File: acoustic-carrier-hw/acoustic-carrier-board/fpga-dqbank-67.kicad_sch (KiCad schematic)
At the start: 14 parts, among them IC1 ECP5-BGA256, Y4 Crystal Oscillator

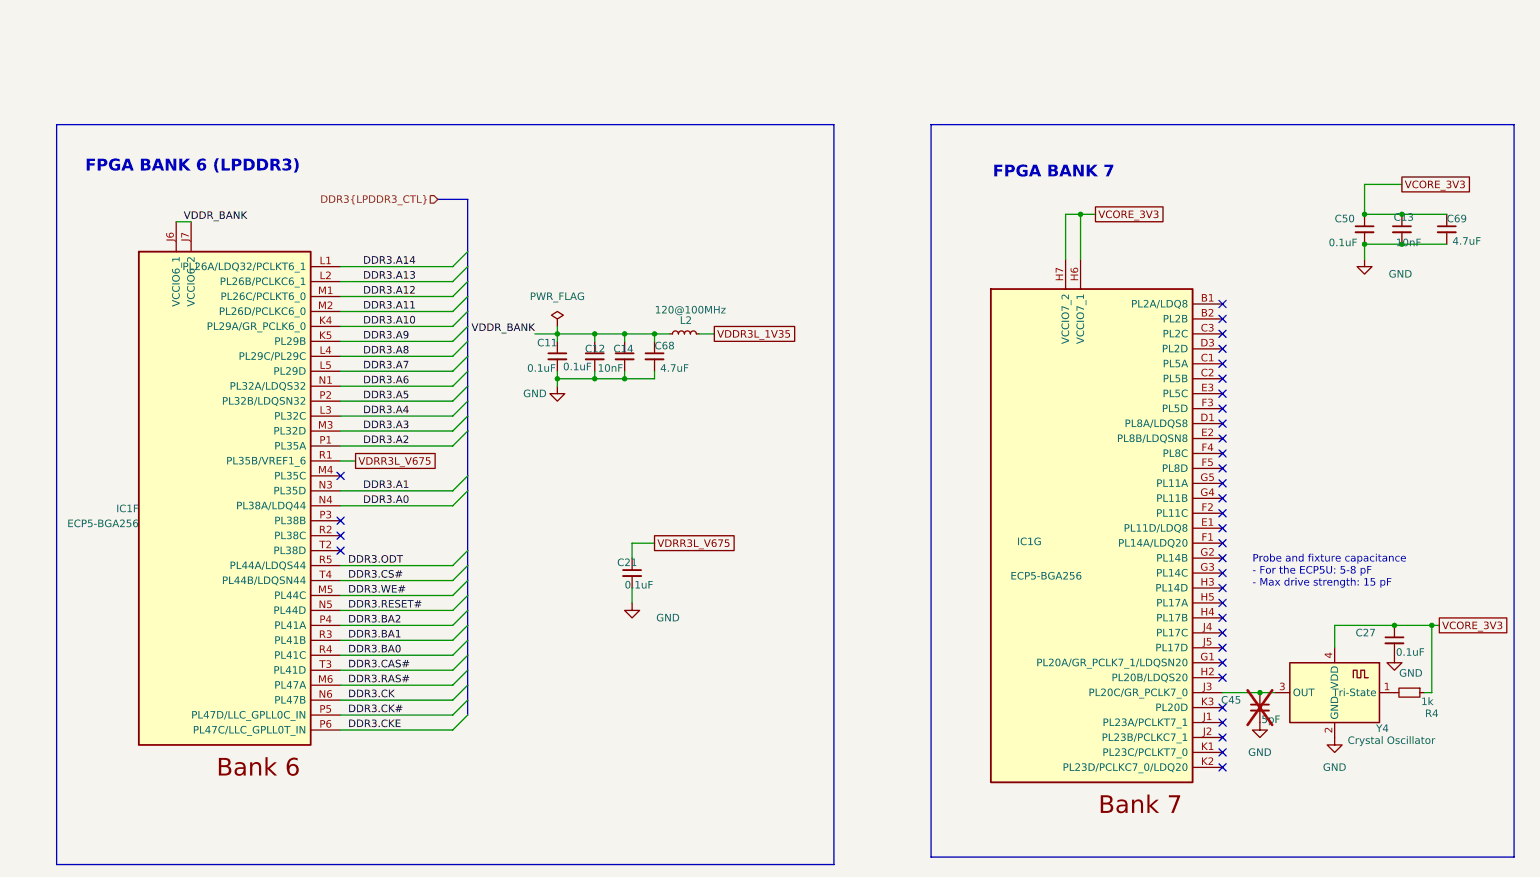
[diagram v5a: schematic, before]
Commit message: [carrier] Finished rough layout, p (put together according to component category
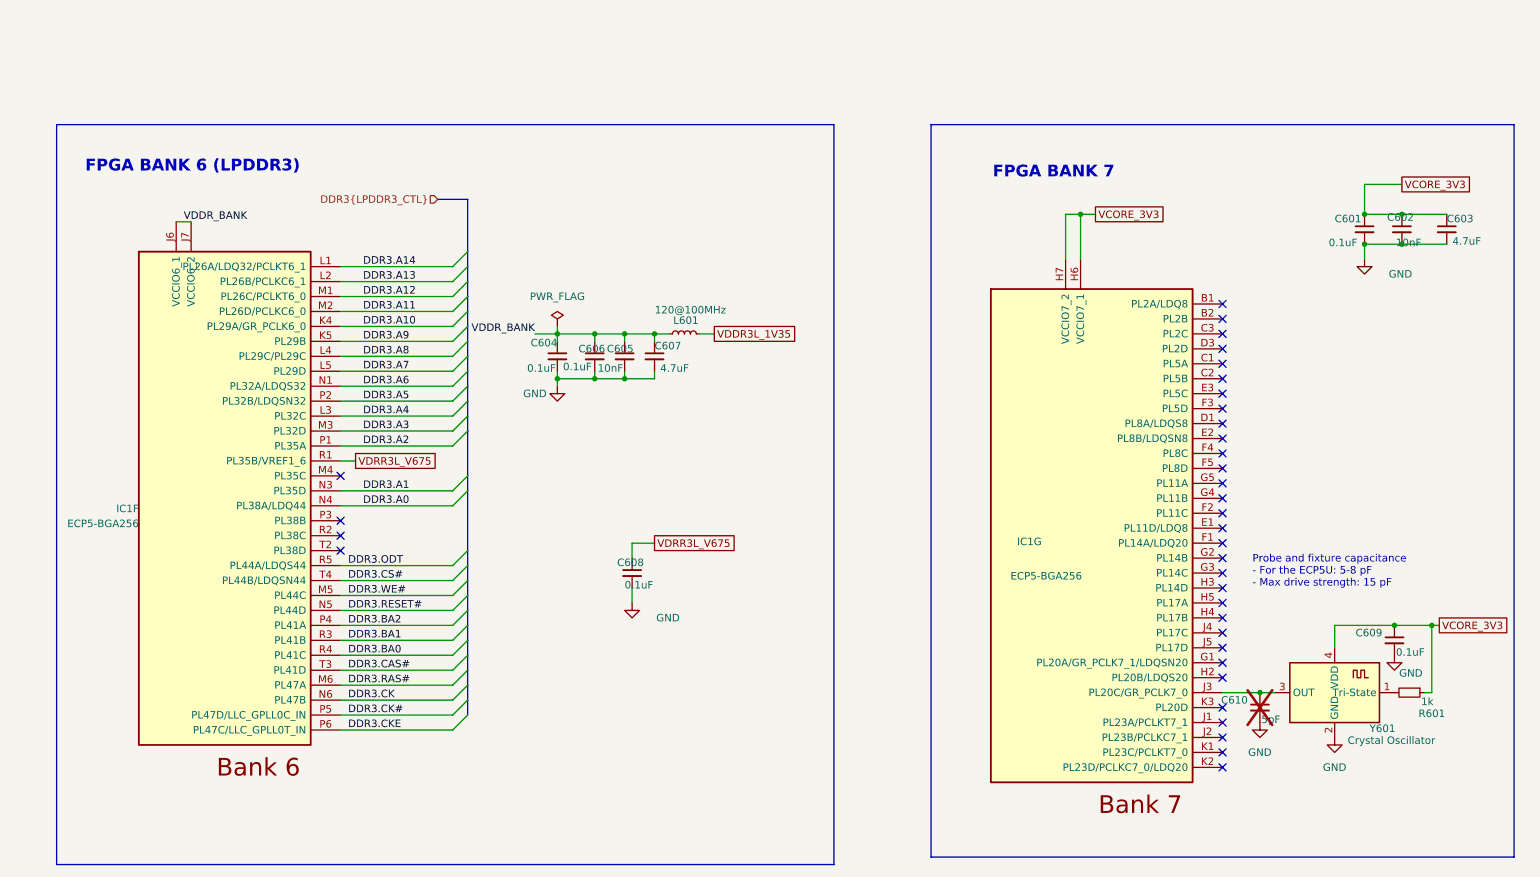
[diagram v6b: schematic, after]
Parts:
- renumbered C50 to C601, C13 to C602, C69 to C603, C11 to C604, C14 to C605, C12 to C606, C68 to C607, C21 to C608, C27 to C609, C45 to C610, L2 to L601, R4 to R601, Y4 to Y601
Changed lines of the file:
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@@
 		(dnp no)
 		(fields_autoplaced yes)
-		(property "Reference" "#PWR012"
+		(property "Reference" "#PWR0605"
 			(at 227.33 140.97 0)
 			(effects
@@
 			(project "acoustic-carrier-board"
 				(path "/25b015c9-ab13-4427-b72c-b6f348597100/9b4bf25f-717e-478b-8aa4-28cd7b267efe"
-					(reference "#PWR012")
+					(reference "#PWR0605")
 					(unit 1)
 				)
@@
 		(on_board yes)
 		(dnp no)
-		(property "Reference" "C12"
+		(property "Reference" "C606"
 			(at 116.078 71.12 0)
 			(effects
@@
 			(project "acoustic-carrier-board"
 				(path "/25b015c9-ab13-4427-b72c-b6f348597100/9b4bf25f-717e-478b-8aa4-28cd7b267efe"
-					(reference "C12")
+					(reference "C606")
 					(unit 1)
 				)
@@
 		(on_board yes)
 		(dnp no)
-		(property "Reference" "C69"
+		(property "Reference" "C603"
 			(at 259.08 49.022 0)
 			(effects
@@
 			(project "acoustic-carrier-board"
 				(path "/25b015c9-ab13-4427-b72c-b6f348597100/9b4bf25f-717e-478b-8aa4-28cd7b267efe"
-					(reference "C69")
+					(reference "C603")
 					(unit 1)
 				)
@@
 		(on_board yes)
 		(dnp no)
-		(property "Reference" "C21"
+		(property "Reference" "C608"
 			(at 118.11 107.442 0)
 			(effects
@@
 			(project "acoustic-carrier-board"
 				(path "/25b015c9-ab13-4427-b72c-b6f348597100/9b4bf25f-717e-478b-8aa4-28cd7b267efe"
-					(reference "C21")
+					(reference "C608")
 					(unit 1)
 				)
@@
 		(dnp no)
 		(fields_autoplaced yes)
-		(property "Reference" "#FLG01"
+		(property "Reference" "#FLG0601"
 			(at 107.95 65.405 0)
 			(effects
@@
 			(project "acoustic-carrier-board"
 				(path "/25b015c9-ab13-4427-b72c-b6f348597100/9b4bf25f-717e-478b-8aa4-28cd7b267efe"
-					(reference "#FLG01")
+					(reference "#FLG0601")
 					(unit 1)
 				)
@@
 		(on_board yes)
 		(dnp no)
-		(property "Reference" "#PWR07"
+		(property "Reference" "#PWR0603"
 			(at 120.65 120.65 0)
 			(effects
@@
 			(project "acoustic-carrier-board"
 				(path "/25b015c9-ab13-4427-b72c-b6f348597100/9b4bf25f-717e-478b-8aa4-28cd7b267efe"
-					(reference "#PWR07")
+					(reference "#PWR0603")
 					(unit 1)
 				)
@@
 		(on_board yes)
 		(dnp no)
-		(property "Reference" "C27"
+		(property "Reference" "C609"
 			(at 243.586 119.38 0)
 			(effects
@@
 			(project "acoustic-carrier-board"
 				(path "/25b015c9-ab13-4427-b72c-b6f348597100/9b4bf25f-717e-478b-8aa4-28cd7b267efe"
-					(reference "C27")
+					(reference "C609")
 					(unit 1)
 				)
@@
 		(on_board yes)
 		(dnp no)
-		(property "Reference" "C14"
+		(property "Reference" "C605"
 			(at 120.904 71.12 0)
 			(effects
@@
 			(project "acoustic-carrier-board"
 				(path "/25b015c9-ab13-4427-b72c-b6f348597100/9b4bf25f-717e-478b-8aa4-28cd7b267efe"
-					(reference "C14")
+					(reference "C605")
 					(unit 1)
 				)
@@
 		(on_board yes)
 		(dnp no)
-		(property "Reference" "Y4"
+		(property "Reference" "Y601"
 			(at 248.158 135.636 0)
 			(effects
@@
 			(project "acoustic-carrier-board"
 				(path "/25b015c9-ab13-4427-b72c-b6f348597100/9b4bf25f-717e-478b-8aa4-28cd7b267efe"
-					(reference "Y4")
+					(reference "Y601")
 					(unit 1)
 				)
@@
 		(dnp no)
 		(fields_autoplaced yes)
-		(property "Reference" "#PWR013"
+		(property "Reference" "#PWR0606"
 			(at 240.03 143.51 0)
 			(effects
@@
 			(project "acoustic-carrier-board"
 				(path "/25b015c9-ab13-4427-b72c-b6f348597100/9b4bf25f-717e-478b-8aa4-28cd7b267efe"
-					(reference "#PWR013")
+					(reference "#PWR0606")
 					(unit 1)
 				)
@@
 		(on_board yes)
 		(dnp no)
-		(property "Reference" "C11"
+		(property "Reference" "C604"
 			(at 107.95 70.104 0)
 			(effects
@@
 			(project "acoustic-carrier-board"
 				(path "/25b015c9-ab13-4427-b72c-b6f348597100/9b4bf25f-717e-478b-8aa4-28cd7b267efe"
-					(reference "C11")
+					(reference "C604")
 					(unit 1)
 				)
@@
 		(on_board yes)
 		(dnp no)
-		(property "Reference" "#PWR011"
+		(property "Reference" "#PWR0604"
 			(at 250.19 129.54 0)
 			(effects
@@
 			(project "acoustic-carrier-board"
 				(path "/25b015c9-ab13-4427-b72c-b6f348597100/9b4bf25f-717e-478b-8aa4-28cd7b267efe"
-					(reference "#PWR011")
+					(reference "#PWR0604")
 					(unit 1)
 				)
@@
 		(on_board yes)
 		(dnp no)
-		(property "Reference" "#PWR05"
+		(property "Reference" "#PWR0602"
 			(at 107.95 83.82 0)
 			(effects
@@
 			(project "acoustic-carrier-board"
 				(path "/25b015c9-ab13-4427-b72c-b6f348597100/9b4bf25f-717e-478b-8aa4-28cd7b267efe"
-					(reference "#PWR05")
+					(reference "#PWR0602")
 					(unit 1)
 				)
@@
 		(on_board yes)
 		(dnp no)
-		(property "Reference" "C50"
+		(property "Reference" "C601"
 			(at 240.03 49.022 0)
 			(effects
@@
 			(project "acoustic-carrier-board"
 				(path "/25b015c9-ab13-4427-b72c-b6f348597100/9b4bf25f-717e-478b-8aa4-28cd7b267efe"
-					(reference "C50")
+					(reference "C601")
 					(unit 1)
 				)
@@
 		(on_board yes)
 		(dnp no)
-		(property "Reference" "#PWR017"
+		(property "Reference" "#PWR0601"
 			(at 245.11 62.23 0)
 			(effects
@@
 			(project "acoustic-carrier-board"
 				(path "/25b015c9-ab13-4427-b72c-b6f348597100/9b4bf25f-717e-478b-8aa4-28cd7b267efe"
-					(reference "#PWR017")
+					(reference "#PWR0601")
 					(unit 1)
 				)
@@
 		(on_board yes)
 		(dnp yes)
-		(property "Reference" "C45"
+		(property "Reference" "C610"
 			(at 220.726 130.81 0)
 			(effects
@@
 			(project "acoustic-carrier-board"
 				(path "/25b015c9-ab13-4427-b72c-b6f348597100/9b4bf25f-717e-478b-8aa4-28cd7b267efe"
-					(reference "C45")
+					(reference "C610")
 					(unit 1)
 				)
@@
 		(on_board yes)
 		(dnp no)
-		(property "Reference" "C68"
+		(property "Reference" "C607"
 			(at 124.46 70.612 0)
 			(effects
@@
 			(project "acoustic-carrier-board"
 				(path "/25b015c9-ab13-4427-b72c-b6f348597100/9b4bf25f-717e-478b-8aa4-28cd7b267efe"
-					(reference "C68")
+					(reference "C607")
 					(unit 1)
 				)
@@
 		(on_board yes)
 		(dnp no)
-		(property "Reference" "L2"
+		(property "Reference" "L601"
 			(at 129.794 66.294 90)
 			(effects
@@
 			(project "acoustic-carrier-board"
 				(path "/25b015c9-ab13-4427-b72c-b6f348597100/9b4bf25f-717e-478b-8aa4-28cd7b267efe"
-					(reference "L2")
+					(reference "L601")
 					(unit 1)
 				)
@@
 		(on_board yes)
 		(dnp no)
-		(property "Reference" "C13"
+		(property "Reference" "C602"
 			(at 253.492 48.768 0)
 			(effects
@@
 			(project "acoustic-carrier-board"
 				(path "/25b015c9-ab13-4427-b72c-b6f348597100/9b4bf25f-717e-478b-8aa4-28cd7b267efe"
-					(reference "C13")
+					(reference "C602")
 					(unit 1)
 				)
@@
 		(on_board yes)
 		(dnp no)
-		(property "Reference" "R4"
+		(property "Reference" "R601"
 			(at 256.54 133.096 90)
 			(effects
@@
 			(project "acoustic-carrier-board"
 				(path "/25b015c9-ab13-4427-b72c-b6f348597100/9b4bf25f-717e-478b-8aa4-28cd7b267efe"
-					(reference "R4")
+					(reference "R601")
 					(unit 1)
 				)

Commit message: [¢arrier] Added netties and determined trace geometry for 50 ohms SE / 100 ohms DIFF impedance (next) reset the appropriate DQS group signals, RGMII and USB signals
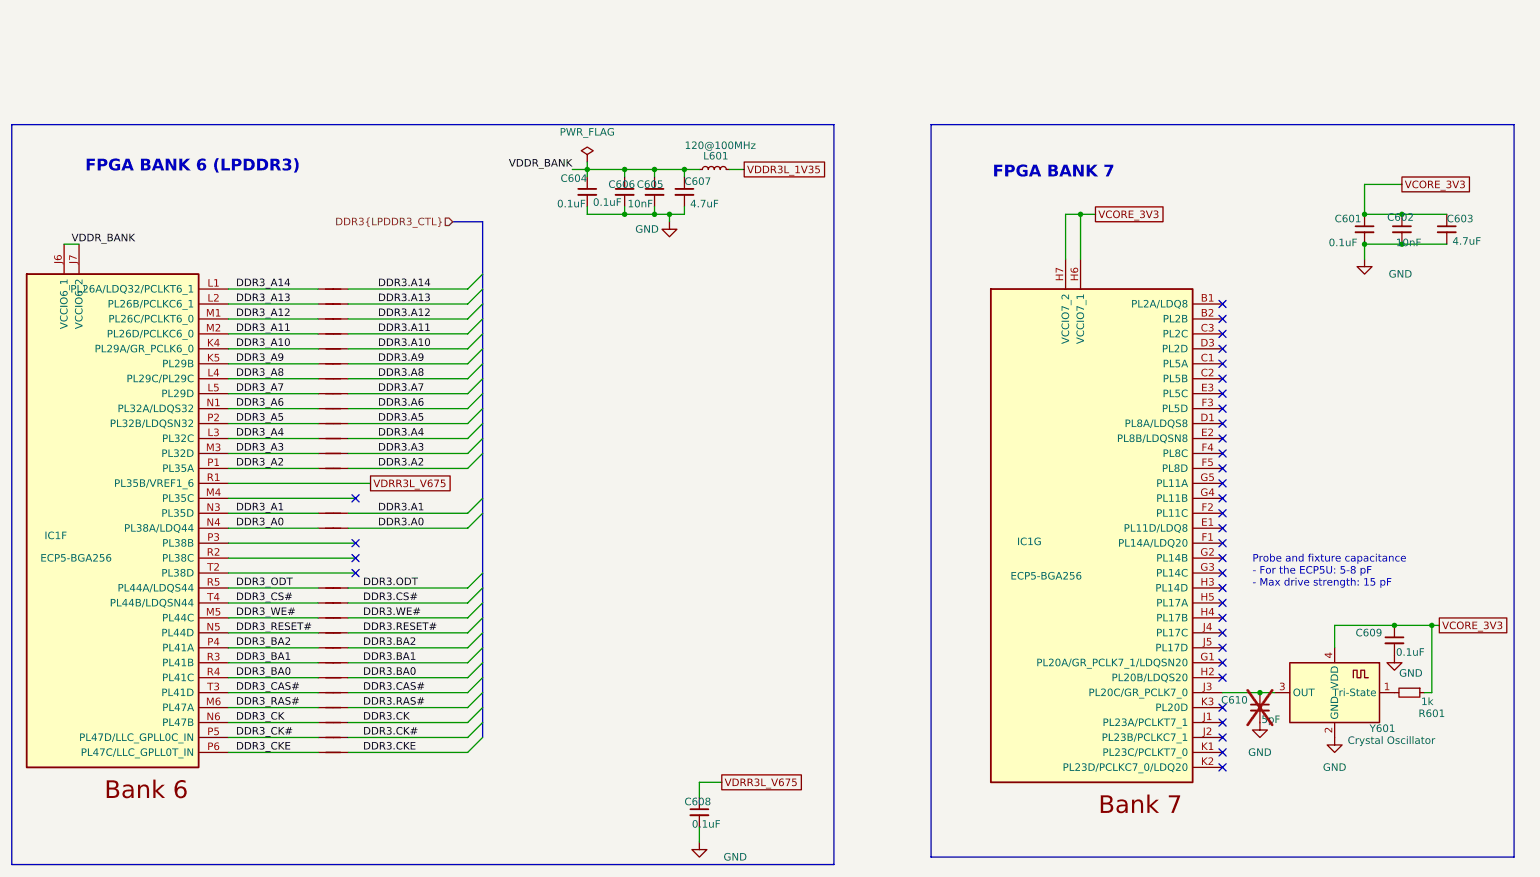
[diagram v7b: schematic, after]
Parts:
- added NT601, NT602, NT603, NT604, NT605, NT606, NT607, NT608, NT609, NT610, NT613, NT614, NT615, NT616, NT617, NT618, NT619, NT620, NT621, NT622, NT623, NT624, NT625, NT626, NT627: NetTie_2, iw-misc:NetTie-2_SMD_Pad0.1565mm, symbol Device:NetTie_2
- added NT611, NT612: NetTie_2, iw-misc:NetTie-2_SMD_Pad0.1240mm, symbol Device:NetTie_2
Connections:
- net DDR3.A0: now also NT627.2; no longer IC1.N4 (PL38A/LDQ44)
- net DDR3.A1: now also NT626.2; no longer IC1.N3 (PL35D)
- net DDR3.A10: now also NT617.2; no longer IC1.K4 (PL29A/GR_PCLK6_0)
- net DDR3.A11: now also NT616.2; no longer IC1.M2 (PL26D/PCLKC6_0)
- net DDR3.A12: now also NT615.2; no longer IC1.M1 (PL26C/PCLKT6_0)
- net DDR3.A13: now also NT614.2; no longer IC1.L2 (PL26B/PCLKC6_1)
- net DDR3.A14: now also NT613.2; no longer IC1.L1 (PL26A/LDQ32/PCLKT6_1)
- net DDR3.A2: now also NT625.2; no longer IC1.P1 (PL35A)
- net DDR3.A3: now also NT624.2; no longer IC1.M3 (PL32D)
- net DDR3.A4: now also NT623.2; no longer IC1.L3 (PL32C)
- net DDR3.A5: now also NT622.2; no longer IC1.P2 (PL32B/LDQSN32)
- net DDR3.A6: now also NT621.2; no longer IC1.N1 (PL32A/LDQS32)
- net DDR3.A7: now also NT620.2; no longer IC1.L5 (PL29D)
- net DDR3.A8: now also NT619.2; no longer IC1.L4 (PL29C/PL29C)
- net DDR3.A9: now also NT618.2; no longer IC1.K5 (PL29B)
- net DDR3.BA0: now also NT607.2; no longer IC1.R4 (PL41C)
- net DDR3.BA1: now also NT606.2; no longer IC1.R3 (PL41B)
- net DDR3.BA2: now also NT605.2; no longer IC1.P4 (PL41A)
- net DDR3.CAS#: now also NT608.2; no longer IC1.T3 (PL41D)
- net DDR3.CK: now also NT611.2; no longer IC1.N6 (PL47B)
- net DDR3.CK#: now also NT612.2; no longer IC1.P5 (PL47D/LLC_GPLL0C_IN)
- net DDR3.CKE: now also NT610.2; no longer IC1.P6 (PL47C/LLC_GPLL0T_IN)
- net DDR3.CS#: now also NT602.2; no longer IC1.T4 (PL44B/LDQSN44)
- net DDR3.ODT: now also NT601.2; no longer IC1.R5 (PL44A/LDQS44)
- net DDR3.RAS#: now also NT609.2; no longer IC1.M6 (PL47A)
- net DDR3.RESET#: now also NT604.2; no longer IC1.N5 (PL44D)
- net DDR3.WE#: now also NT603.2; no longer IC1.M5 (PL44C)
- new net DDR3_A0: IC1.N4 (PL38A/LDQ44), NT627.1
- new net DDR3_A1: IC1.N3 (PL35D), NT626.1
- new net DDR3_A10: IC1.K4 (PL29A/GR_PCLK6_0), NT617.1
- new net DDR3_A11: IC1.M2 (PL26D/PCLKC6_0), NT616.1
- new net DDR3_A12: IC1.M1 (PL26C/PCLKT6_0), NT615.1
- new net DDR3_A13: IC1.L2 (PL26B/PCLKC6_1), NT614.1
- new net DDR3_A14: IC1.L1 (PL26A/LDQ32/PCLKT6_1), NT613.1
- new net DDR3_A2: IC1.P1 (PL35A), NT625.1
- new net DDR3_A3: IC1.M3 (PL32D), NT624.1
- new net DDR3_A4: IC1.L3 (PL32C), NT623.1
- new net DDR3_A5: IC1.P2 (PL32B/LDQSN32), NT622.1
- new net DDR3_A6: IC1.N1 (PL32A/LDQS32), NT621.1
- new net DDR3_A7: IC1.L5 (PL29D), NT620.1
- new net DDR3_A8: IC1.L4 (PL29C/PL29C), NT619.1
- new net DDR3_A9: IC1.K5 (PL29B), NT618.1
- new net DDR3_BA0: IC1.R4 (PL41C), NT607.1
- new net DDR3_BA1: IC1.R3 (PL41B), NT606.1
- new net DDR3_BA2: IC1.P4 (PL41A), NT605.1
- new net DDR3_CAS#: IC1.T3 (PL41D), NT608.1
- new net DDR3_CK: IC1.N6 (PL47B), NT611.1
- new net DDR3_CK#: IC1.P5 (PL47D/LLC_GPLL0C_IN), NT612.1
- new net DDR3_CKE: IC1.P6 (PL47C/LLC_GPLL0T_IN), NT610.1
- new net DDR3_CS#: IC1.T4 (PL44B/LDQSN44), NT602.1
- new net DDR3_ODT: IC1.R5 (PL44A/LDQS44), NT601.1
- new net DDR3_RAS#: IC1.M6 (PL47A), NT609.1
- new net DDR3_RESET#: IC1.N5 (PL44D), NT604.1
- new net DDR3_WE#: IC1.M5 (PL44C), NT603.1
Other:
- moved on the sheet: C604, C605, C606, C607, C608, IC1F, L601
